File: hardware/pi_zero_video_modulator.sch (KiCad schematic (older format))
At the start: 44 parts, among them J1 RPi_GPIO, J2 Pi Video, J3 Conn_Coaxial, SW1 SW_SPDT, U1 NJM2519A

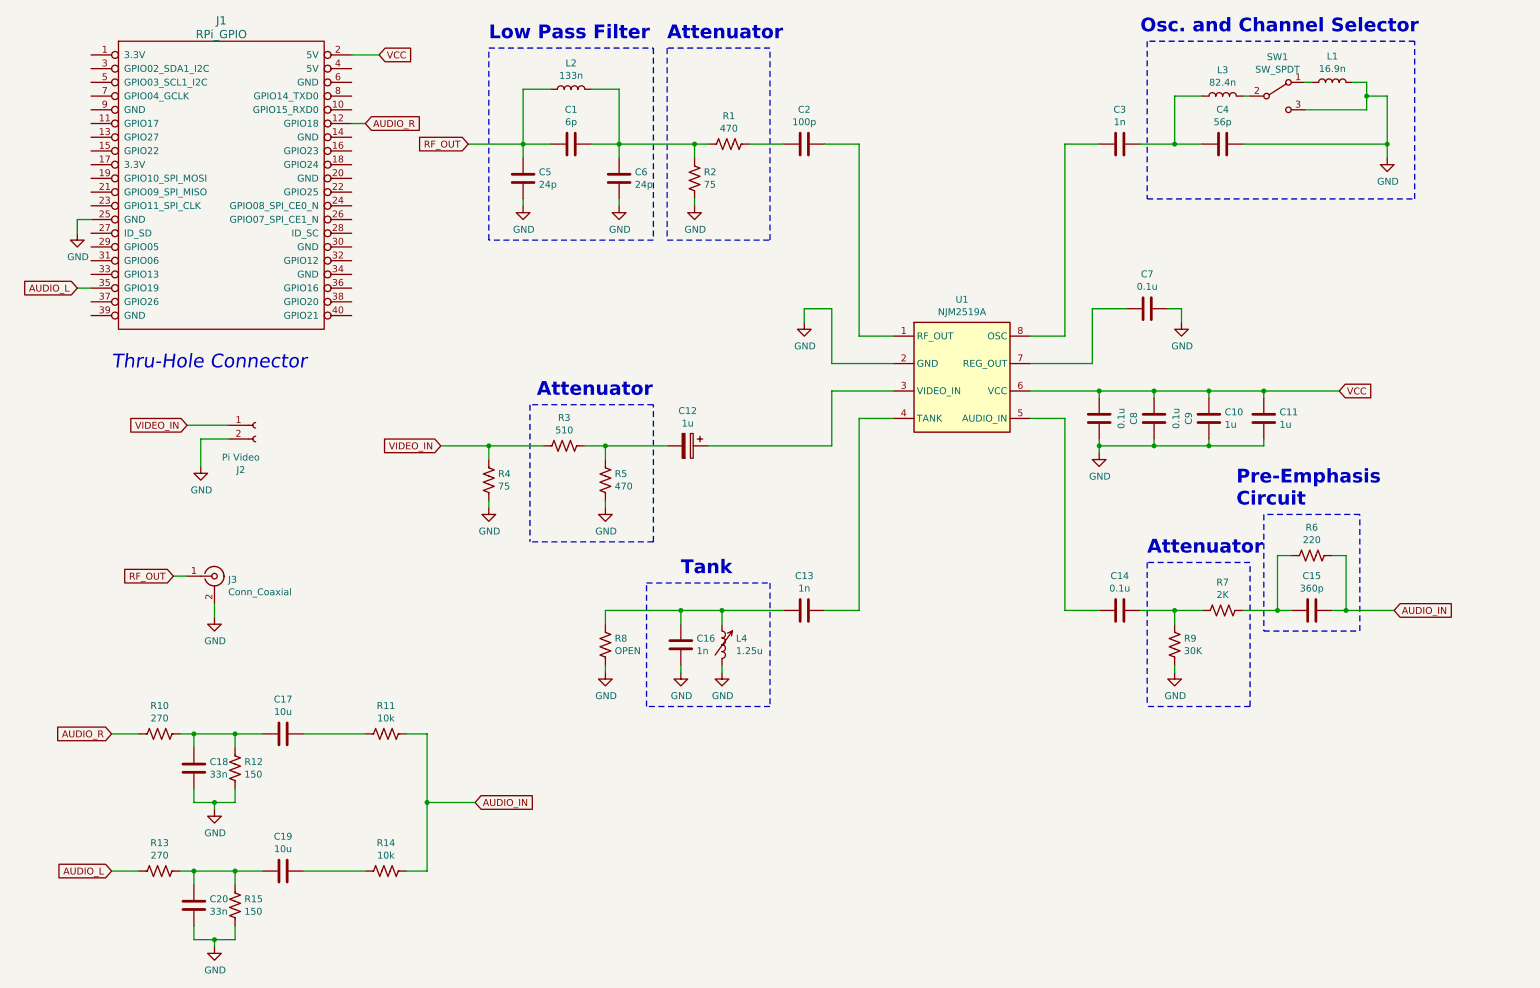
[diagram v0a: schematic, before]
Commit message: Added PLL to schematic
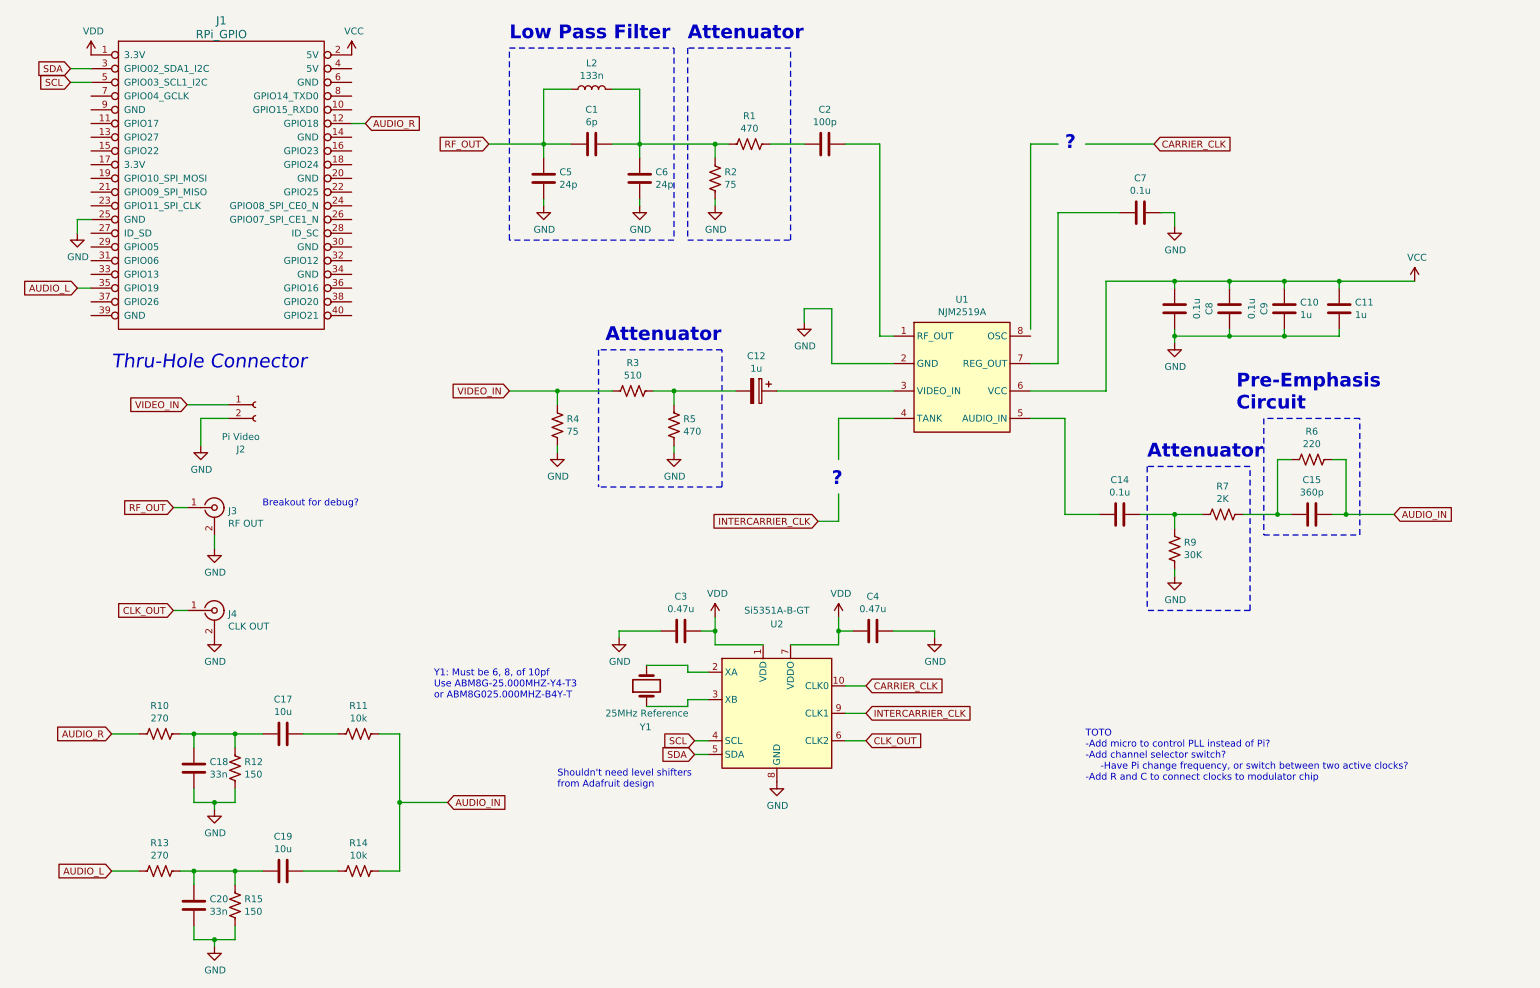
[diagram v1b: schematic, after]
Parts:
- removed C13, C16: 1n, Capacitor_SMD:C_0805_2012Metric, symbol Device:C
- removed L1: 16.9n, Inductor_SMD:L_0603_1608Metric, symbol Device:L
- removed L3: 82.4n, Inductor_SMD:L_0603_1608Metric, symbol Device:L
- removed L4: 1.25u, KiCad-Library-master:143-18J12L, symbol Device:LTRIM
- removed R8: OPEN, Resistor_SMD:R_0805_2012Metric, symbol Device:R_US
- removed SW1: SW_SPDT, Button_Switch_SMD:SW_SPDT_PCM12, symbol Switch:SW_SPDT
- added J4: CLK OUT, symbol Connector:Conn_Coaxial
- added U2: Si5351A-B-GT, Package_SO:MSOP-10_3x3mm_P0.5mm, symbol Oscillator:Si5351A-B-GT
- added Y1: 25MHz Reference, symbol Device:Crystal
- C3: value 1n -> 0.47u; footprint Capacitor_SMD:C_0805_2012Metric -> (none)
- C4: value 56p -> 0.47u; footprint Capacitor_SMD:C_0805_2012Metric -> (none)
- J3: value Conn_Coaxial -> RF OUT
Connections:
- net labels added: CARRIER_CLK, CLK_OUT, INTERCARRIER_CLK, SCL, SDA, VDD
- wire segments 139 -> 142
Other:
- note added: "?"
- note added: "Breakout for debug?"
- note added: "Shouldn't need level shifters\nfrom Adafruit design"
- note added: "TOTO\n-Add micro to control PLL instead of Pi?\n-Add channel selector switch?\n -Have Pi change frequency, or switch between two active clocks?\n-Add R and C to connect clocks to modulator chip"
- note added: "Y1: Must be 6, 8, of 10pf\nUse ABM8G-25.000MHZ-Y4-T3\nor ABM8G025.000MHZ-B4Y-T"
- note removed: "Osc. and Channel Selector"
- note removed: "Tank"
- moved on the sheet: C1, C10, C11, C12, C14, C15, C2, C5, C6, C7, C8, C9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

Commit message: Connected Clocks in Schematic
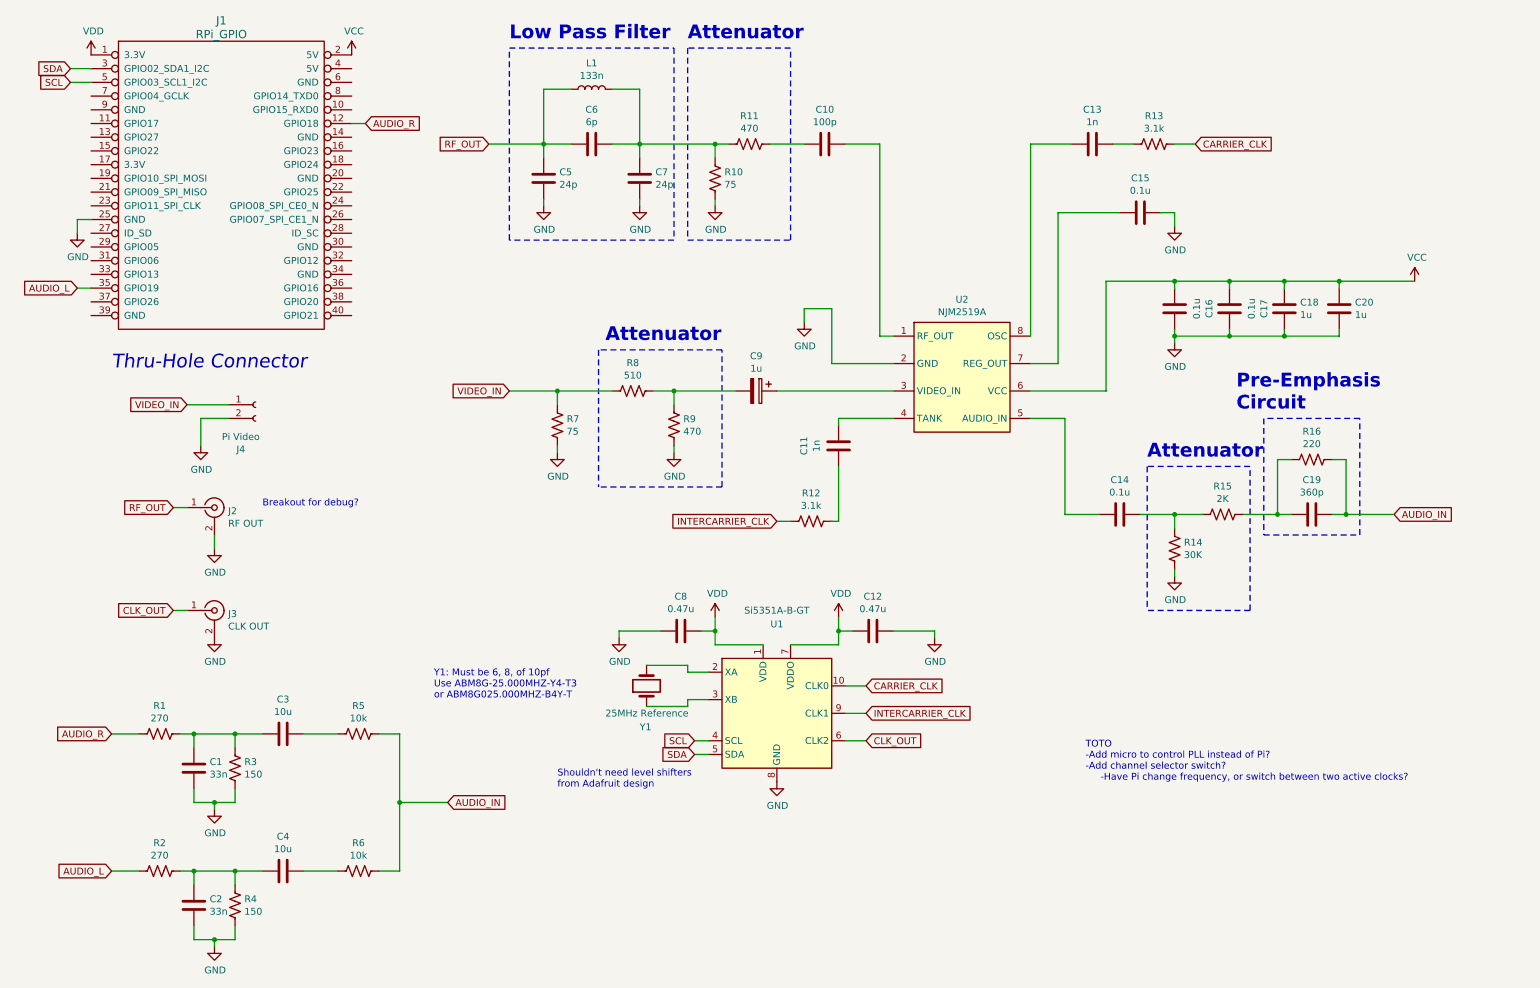
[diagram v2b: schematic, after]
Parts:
- added C11, C13: 1n, symbol Device:C
- added R12, R13: 3.1k, symbol Device:R_US
- renumbered C18 to C1, C2 to C10, C4 to C12, C7 to C15, C8 to C16, C9 to C17, C10 to C18, C15 to C19, C20 to C2, C11 to C20, C17 to C3, C19 to C4, C1 to C6, C6 to C7, C3 to C8, C12 to C9, J3 to J2, J4 to J3, J2 to J4, L2 to L1, R10 to R1, R2 to R10, R1 to R11, R9 to R14, R7 to R15, R6 to R16, R13 to R2, R12 to R3, R15 to R4, R11 to R5, R14 to R6, R4 to R7, R3 to R8, R5 to R9, U2 to U1, U1 to U2
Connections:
- wire segments 142 -> 144
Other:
- note added: "TOTO\n-Add micro to control PLL instead of Pi?\n-Add channel selector switch?\n -Have Pi change frequency, or switch between two active clocks?"
- note removed: "?"
- note removed: "TOTO\n-Add micro to control PLL instead of Pi?\n-Add channel selector switch?\n -Have Pi change frequency, or switch between two active clocks?\n-Add R and C to connect clocks to modulator chip"

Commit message: Updates
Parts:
- removed C12, C8: 0.47u, symbol Device:C
- removed J3: CLK OUT, symbol Connector:Conn_Coaxial
- removed R12, R13: 3.1k, symbol Device:R_US
- removed U1: Si5351A-B-GT, Package_SO:MSOP-10_3x3mm_P0.5mm, symbol Oscillator:Si5351A-B-GT
- removed Y1: 25MHz Reference, symbol Device:Crystal
- added C15: 68p, Capacitor_SMD:C_0805_2012Metric, symbol Device:C
- added L2: LTRIM, rf_modulator:Coilcraft Slot 7 Inductor, symbol Device:LTRIM
- added R9: R_US, Resistor_SMD:R_0805_2012Metric, symbol Device:R_US
- added SW1: SW_SPDT, Button_Switch_SMD:SW_SPDT_PCM12, symbol Switch:SW_SPDT
- added X1: F88SM, rf_modulator:F88SM, symbol rfmod:F88SM
- C1: renamed from C6; Material Type (none) -> C0G; Tolerance (none) -> 10%; Voltage (none) -> 50V
- C10: renamed from C20; Material Type (none) -> C0G; Tolerance (none) -> 10%; Voltage (none) -> 50V
- C11: renamed from C9; ESR (none) -> 7; Material Type (none) -> Tantalum; Tolerance (none) -> 10%; Voltage (none) -> 50V
- C12: renamed from C11; footprint (none) -> Capacitor_SMD:C_0805_2012Metric; Material Type (none) -> C0G; Tolerance (none) -> 10%; Voltage (none) -> 50
- C13: renamed from C14; Material Type (none) -> C0G; Tolerance (none) -> 10%; Voltage (none) -> 50V
- C14: renamed from C19; Material Type (none) -> C0G; Tolerance (none) -> 10%; Voltage (none) -> 50V
- C16: renamed from C3; Material Type (none) -> C0G; Tolerance (none) -> 10%; Voltage (none) -> 50V
- C17: renamed from C1; Material Type (none) -> C0G; Tolerance (none) -> 10%; Voltage (none) -> 50V
- C18: renamed from C4; Material Type (none) -> C0G; Tolerance (none) -> 10%; Voltage (none) -> 50V
- C19: renamed from C2; Material Type (none) -> C0G; Tolerance (none) -> 10%; Voltage (none) -> 50V
- C2: renamed from C10; Material Type (none) -> C0G; Tolerance (none) -> 10%; Voltage (none) -> 50V
- C3: renamed from C13; footprint (none) -> Capacitor_SMD:C_0805_2012Metric; Material Type (none) -> C0G; Tolerance (none) -> 10%; Voltage (none) -> 50V
- C4: renamed from C5; Material Type (none) -> C0G; Tolerance (none) -> 10%; Voltage (none) -> 50V
- C5: renamed from C7; Material Type (none) -> C0G; Tolerance (none) -> 10%; Voltage (none) -> 50V
- C6: renamed from C15; Material Type (none) -> C0G; Tolerance (none) -> 10%; Voltage (none) -> 50V
- C7: renamed from C16; Material Type (none) -> C0G; Tolerance (none) -> 10%; Voltage (none) -> 50V
- C8: renamed from C17; Material Type (none) -> C0G; Tolerance (none) -> 10%; Voltage (none) -> 50V
- C9: renamed from C18; Material Type (none) -> C0G; Tolerance (none) -> 10%; Voltage (none) -> 50V
- J1: Part Number (none) -> Adafruit 2222
- J2: renamed from J4; Part Number (none) -> 90147-1102
- J3: renamed from J2; Part Number (none) -> 73330-0030
- L1: Current (none) -> 3A; Part Number (none) -> 744918213; Tolerance (none) -> 5%
- R1: renamed from R11; Power (none) -> 0.125W; Tolerance (none) -> 5%
- R10: renamed from R1; Power (none) -> 0.25W; Tolerance (none) -> 5%
- R11: renamed from R5; Power (none) -> 0.125W; Tolerance (none) -> 5%
- R12: renamed from R3; Power (none) -> 0.25W; Tolerance (none) -> 5%
- R13: renamed from R2; Power (none) -> 0.25W; Tolerance (none) -> 5%
- R14: renamed from R6; Power (none) -> 0.125W; Tolerance (none) -> 5%
- R15: renamed from R4; Power (none) -> 0.25W; Tolerance (none) -> 5%
- R2: renamed from R10; Power (none) -> 0.5W; Tolerance (none) -> 0.5%
- R3: renamed from R8; Power (none) -> 0.125W; Tolerance (none) -> 5%
- R4: renamed from R7; Power (none) -> 0.5W; Tolerance (none) -> 0.5%
- R5: renamed from R9; Power (none) -> 0.125W; Tolerance (none) -> 5%
- R6: renamed from R16; Power (none) -> 0.25 W; Tolerance (none) -> 5%
- R7: renamed from R15; Power (none) -> 0.125W; Tolerance (none) -> 5%
- R8: renamed from R14; Power (none) -> 0.125W; Tolerance (none) -> 5%
- U1: renamed from U2; Part Number (none) -> NJM2519A
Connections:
- net GND: now also C15.1, L2.2, R9.2, X1.3 (GND)
- net at C3.1: now also SW1.2 (B)
- net at C12.2: now also C15.2, L2.1, R9.1
- net SCL: no longer names the net of J1.5 (GPIO03_SCL1_I2C)
- net SDA: no longer names the net of J1.3 (GPIO02_SDA1_I2C)
- new net: SW1.1 (A), X1.1 (LOW)
- new net: SW1.3 (C), X1.2 (HIGH)
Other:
- note added: "4.5MHz Tank"
- note removed: "Shouldn't need level shifters\nfrom Adafruit design"
- note removed: "TOTO\n-Add micro to control PLL instead of Pi?\n-Add channel selector switch?\n -Have Pi change frequency, or switch between two active clocks?"
- note removed: "Y1: Must be 6, 8, of 10pf\nUse ABM8G-25.000MHZ-Y4-T3\nor ABM8G025.000MHZ-B4Y-T"
- moved on the sheet: C1, C10, C11, C12, C13, C14, C2, C3, C4, C5, C6, C7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
